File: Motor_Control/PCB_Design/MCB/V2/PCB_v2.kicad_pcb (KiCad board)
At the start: 2 copper layers, 80.1 x 70 mm, 35 parts, among them J1 Molex_Motor, J2 Conn_Encoder, J3 Molex_Pwr_In, J4 Teensy, J5 Molex_Pwr_Out, J6 Adress_Pins, J9 Conn_I2C, Q1 Q_NMOS_IRLB8743, Q2 Q_NMOS_IRLB8743, Q3 Q_NMOS_IRLB8743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

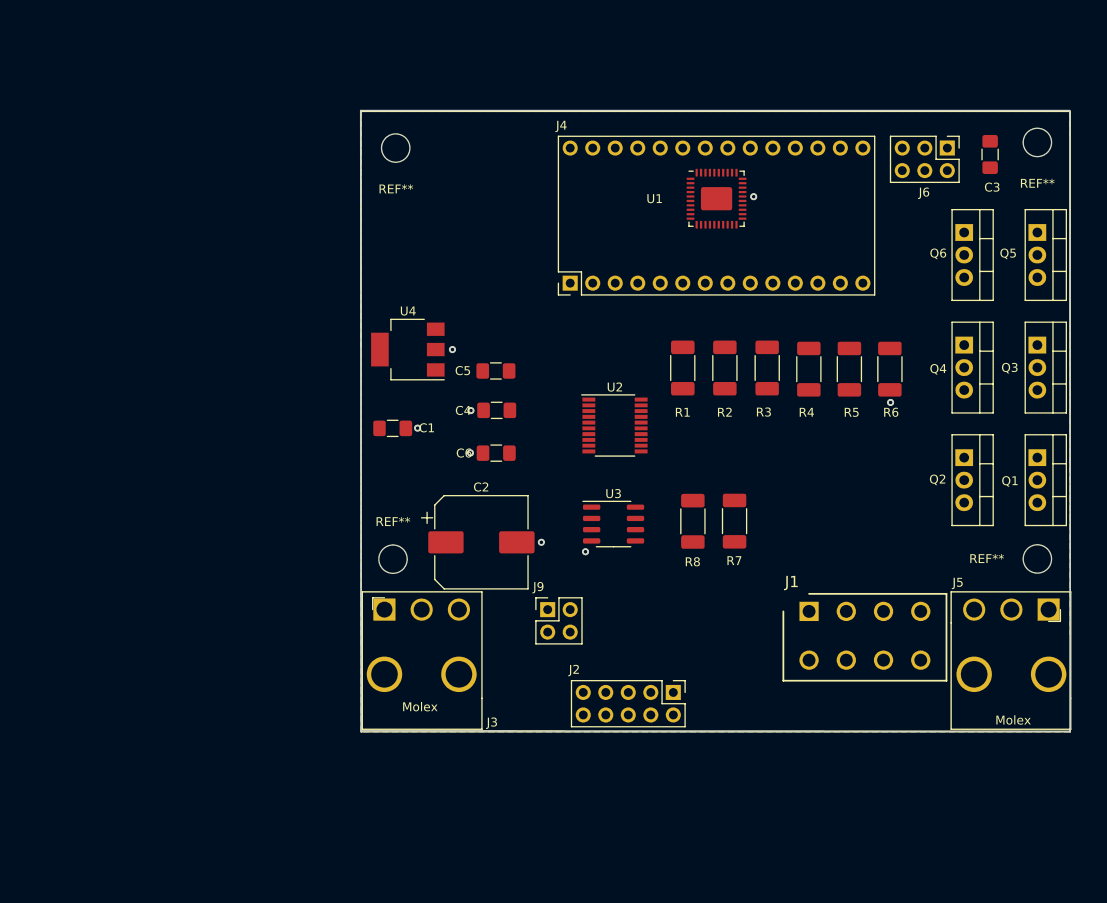
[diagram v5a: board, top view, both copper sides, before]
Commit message: Début tracks
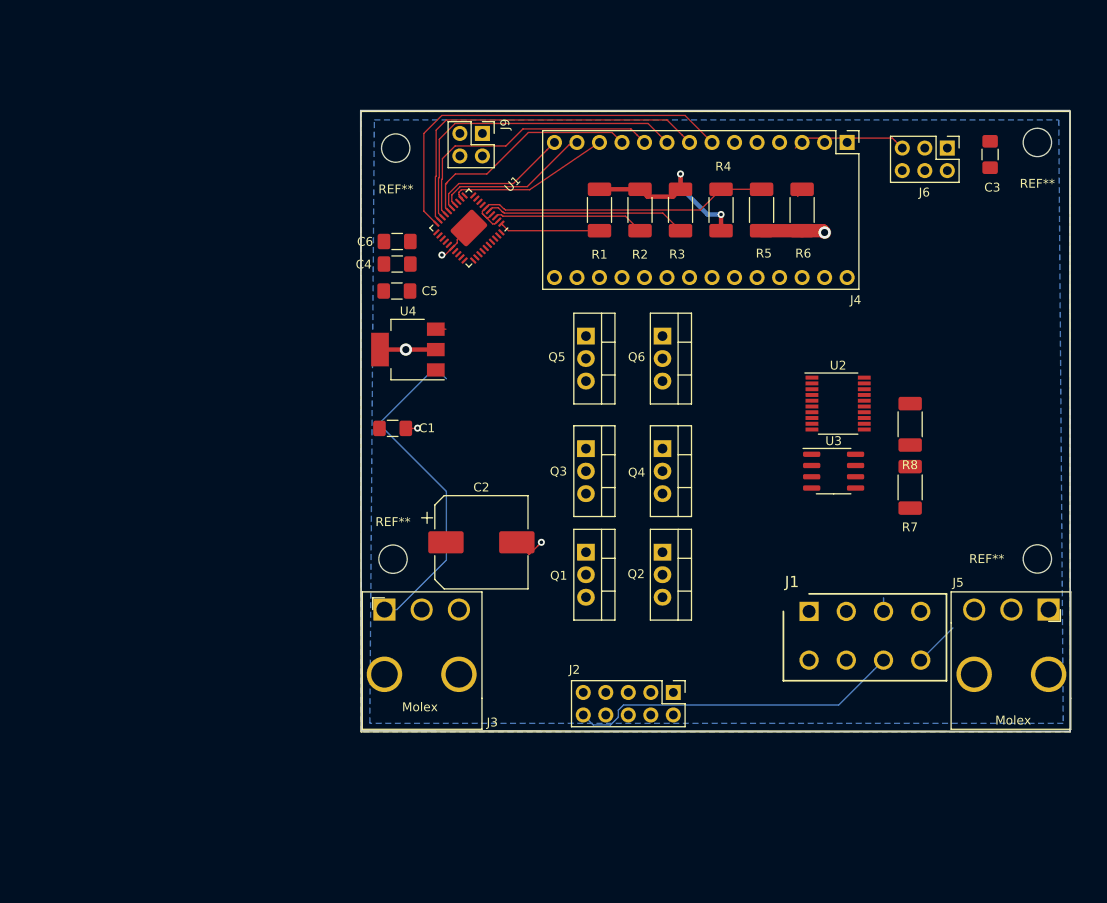
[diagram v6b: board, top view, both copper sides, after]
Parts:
- moved J9 54.2 mm to (138.7, 62.5), turned to 0 degrees
- moved Q3 52.3 mm to (150.4, 98.0)
- moved Q5 52.3 mm to (150.4, 85.3)
- moved Q1 52.0 mm to (150.4, 109.7)
- moved Q4 36.0 mm to (159.0, 98.0)
- moved Q6 36.0 mm to (159.0, 85.3)
- moved Q2 35.7 mm to (159.0, 109.7)
- moved J4 35.0 mm to (179.8, 63.5), turned to 270 degrees
- moved U1 28.1 mm to (137.2, 73.2), turned to 225 degrees
- moved R8 26.8 mm to (186.9, 95.3)
- moved C6 26.4 mm to (129.1, 74.7)
- moved U3 25.5 mm to (178.3, 100.6)
- moved U2 25.3 mm to (178.8, 93.0)
- moved R4 20.5 mm to (165.6, 71.1), turned to 90 degrees
- moved R5 20.5 mm to (170.2, 71.1)
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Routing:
- net /Vreg: track 0.00 -> 58.6 mm, vias 0 -> 2
- net /BRAKE: track 0.00 -> 45.4 mm
- net /CLKIN: track 0.00 -> 40.5 mm
- net /Vm: track 0.00 -> 39.9 mm
- net /UHN: track 0.00 -> 37.1 mm
- net /LOCKn: track 0.00 -> 36.4 mm
- net /FAULTn: track 0.00 -> 31.3 mm
- net /FGOUT: track 0.00 -> 26.3 mm
- net GNDREF: track 0.00 -> 23.2 mm, vias 8 -> 5
- net /Hall_3: track 0.00 -> 22.9 mm
- net /SCS: track 0.00 -> 18.6 mm
- net /DATAI: track 0.00 -> 17.9 mm
- net /Hall_2: track 0.00 -> 17.2 mm
- net /DATAO: track 0.00 -> 16.1 mm
- net /MCU/A2: track 0.00 -> 13.0 mm
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
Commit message: All routs
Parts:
- moved C3 61.8 mm to (136.1, 80.3), turned to 180 degrees
- moved Q2 6.27 mm to (161.3, 115.6), turned to 90 degrees
- moved Q1 6.01 mm to (151.8, 115.6), turned to 90 degrees
- moved J6 5.85 mm to (187.3, 68.6), turned to 0 degrees
- moved Q4 5.34 mm to (161.3, 102.9), turned to 90 degrees
- moved Q6 5.34 mm to (161.3, 90.2), turned to 90 degrees
- moved Q3 5.02 mm to (151.8, 102.9), turned to 90 degrees
- moved Q5 5.02 mm to (151.8, 90.2), turned to 90 degrees
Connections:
- J2 pad 10: /Vreg -> /Vin
- U2 pad 1: /Vreg -> /Vin
- U3 pad 1: /Vreg -> /Vin
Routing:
- net /Vm: track 39.9 -> 181.1 mm, vias 0 -> 4
- net /Vin: track 1.15 -> 124.8 mm, vias 0 -> 4
- net /Power/ISEN: track 1.02 -> 113.7 mm, vias 0 -> 2
- net /ENC_A: track 0.00 -> 75.8 mm
- net Motor_3: track 5.13 -> 79.3 mm
- net Motor_1: track 1.54 -> 74.6 mm
- net Motor_2: track 0.00 -> 72.7 mm
- net /Hall_1: track 11.4 -> 81.0 mm
- net /ENC_B: track 0.00 -> 69.4 mm, vias 0 -> 1
- net /ENC_!A: track 0.00 -> 69.0 mm
- net /RESET: track 0.00 -> 64.8 mm, vias 0 -> 1
- net /ENC_!B: track 0.00 -> 62.0 mm
- net /Hall_2: track 17.2 -> 79.1 mm, vias 0 -> 2
- net /B: track 0.00 -> 54.9 mm
- net /ENABLE: track 0.00 -> 53.4 mm, vias 0 -> 1
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
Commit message: Board finit!
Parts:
- added LOGO: , MyLibrary:logo_metis, F.Cu at (184.8, 78.0)
- C2: footprint Capacitor_SMD:CP_Elec_10x10 -> Capacitor_THT:CP_Radial_D8.0mm_P5.00mm
- R6: footprint Resistor_SMD:R_2010_5025Metric_Pad1.52x2.65mm_HandSolder -> Resistor_SMD:R_2512_6332Metric_Pad1.52x3.35mm_HandSolder
- moved C2 9.29 mm to (130.8, 103.5)
- moved J6 5.72 mm to (193.0, 68.6)
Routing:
- net GNDREF: track 29.1 -> 55.9 mm, vias 9 -> 11
- net /B: track 54.9 -> 64.1 mm, vias 0 -> 1
- net /A: track 45.2 -> 51.8 mm, vias 0 -> 1
- net /MCU/A1: track 38.6 -> 44.3 mm
- net /MCU/A0: track 42.2 -> 47.9 mm
- net /Vm: track 181.1 -> 186.3 mm, vias 4 -> 3
- net /MCU/A2: track 35.7 -> 40.7 mm
- net /Power/ISEN: track 113.7 -> 112.8 mm
- net /Vreg: track 110.4 -> 110.9 mm
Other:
- board text added: "A"
- board text added: "A0"
- board text added: "A1"
- board text added: "A2"
- board text added: "B"
- board text added: "Motor Control Board V2"
